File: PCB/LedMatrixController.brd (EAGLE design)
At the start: 100 x 80 mm, 9 parts, among them IC1 AT90S2313S, IC2 74LS595D

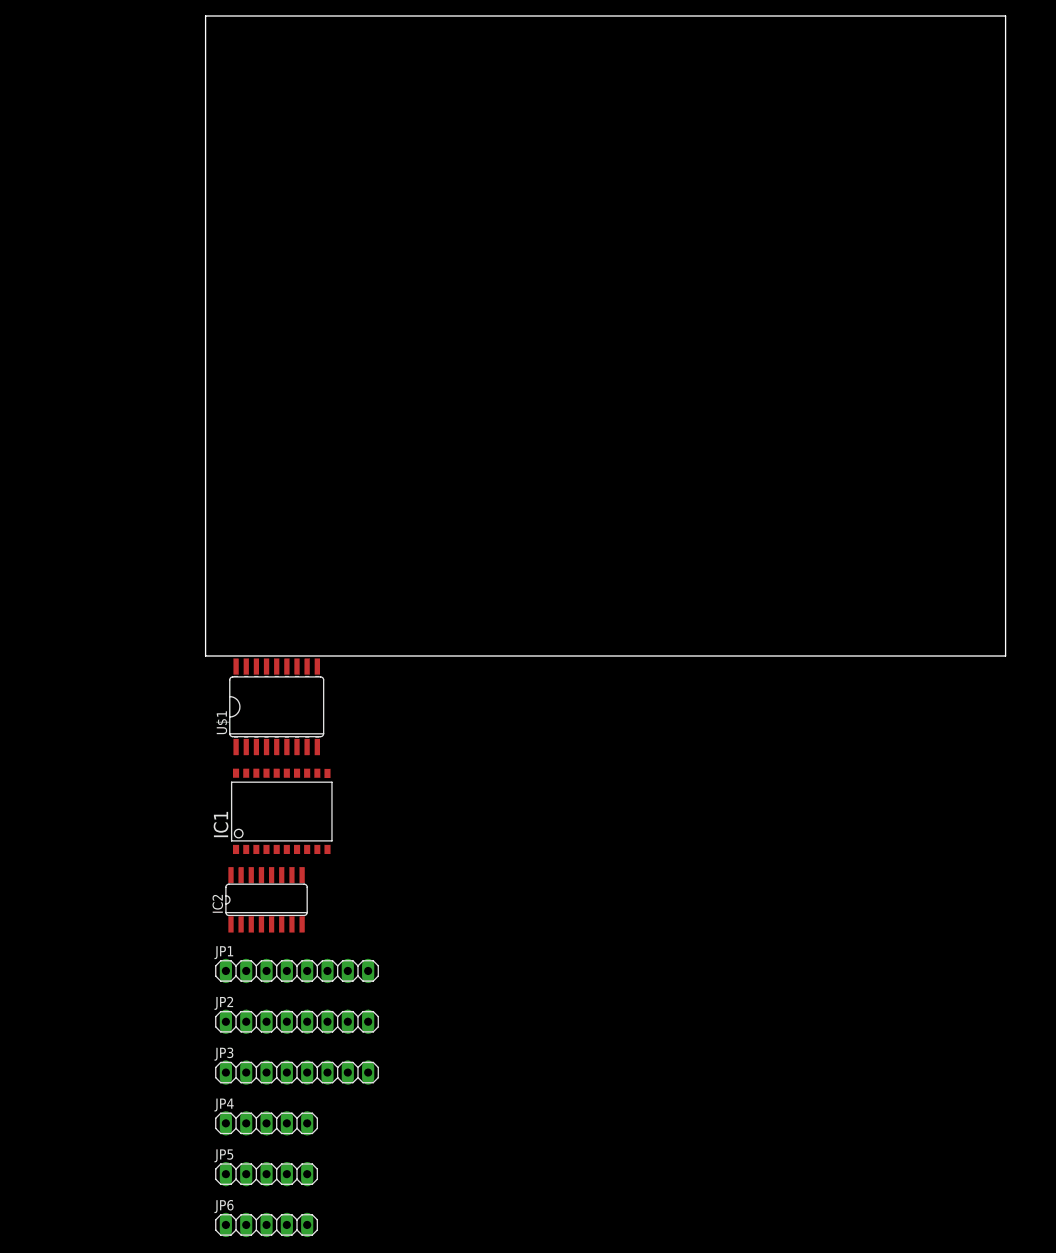
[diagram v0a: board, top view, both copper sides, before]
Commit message: Added connections between main elements. Created dimensions on the pbc layout.
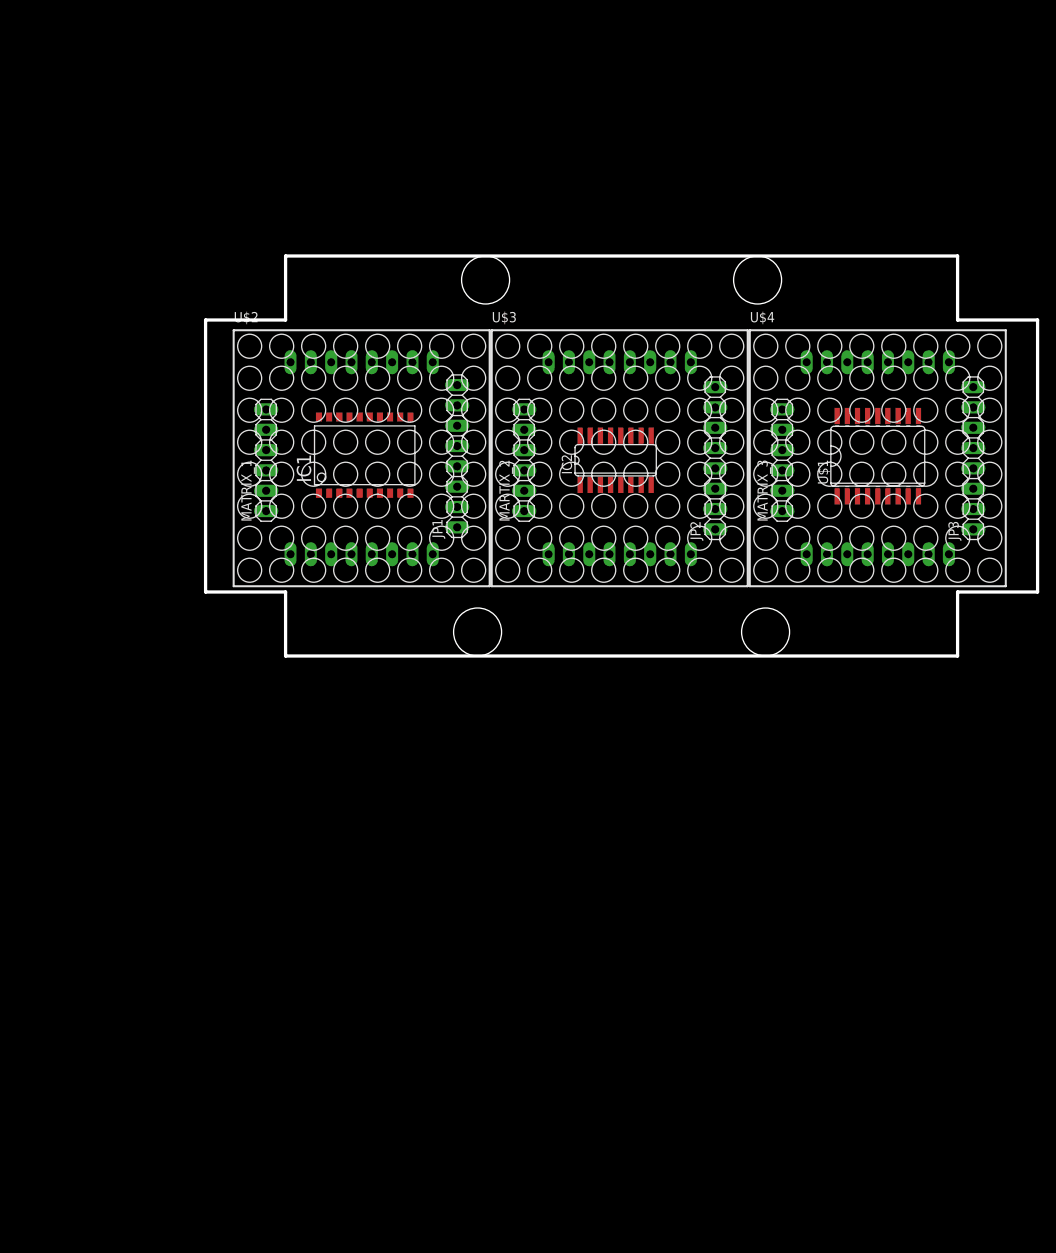
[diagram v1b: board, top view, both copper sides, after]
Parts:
- removed JP4, JP5, JP6: (no value), pinhead:1X05
- added MARTIX_2, MATRIX_1, MATRIX_3: (no value), pinhead:1X06
- added U$2, U$3, U$4: NFM-12881BG-11, led_matrix_8x8:NFM-12881BG-11
- moved JP3 114.2 mm to (96.0, 24.7), turned to 90 degrees
- moved JP2 87.7 mm to (63.7, 24.7), turned to 90 degrees
- moved U$1 81.4 mm to (84.0, 25.0)
- moved IC2 70.2 mm to (51.3, 24.5)
- moved JP1 67.4 mm to (31.4, 25.0), turned to 90 degrees
- moved IC1 45.7 mm to (19.3, 25.5)
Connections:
- new net CLK: IC1.11, MARTIX_2.4, MATRIX_1.4, MATRIX_3.4
- new net N$10: MARTIX_2.3, MATRIX_1.6
- new net N$11: MARTIX_2.6, MATRIX_3.3
- new net N$12: IC1.9, MATRIX_1.3
- new net N$9: IC1.8, MARTIX_2.5, MATRIX_1.5, MATRIX_3.5
- new net R1: IC2.15, U$1.1
- new net R2: IC2.1, U$1.2
- new net R3: IC2.2, U$1.3
- new net R4: IC2.3, U$1.4
- new net R5: IC2.4, U$1.5
- new net R6: IC2.5, U$1.6
- new net R7: IC2.6, U$1.7
- new net R8: IC2.7, U$1.8
- new net ROW1: JP1.1, JP2.1, JP3.1, U$1.10
- new net ROW2: JP1.2, JP2.2, JP3.2, U$1.11
- new net ROW3: JP1.3, JP2.3, JP3.3, U$1.12
- new net ROW4: JP1.4, JP2.4, JP3.4, U$1.13
- new net ROW5: JP1.5, JP2.5, JP3.5, U$1.14
- new net ROW6: JP1.6, JP2.6, JP3.6, U$1.15
- new net ROW7: JP1.7, JP2.7, JP3.7, U$1.16
- new net ROW8: JP1.8, JP2.8, JP3.8, U$1.17
- net GND: now also MARTIX_2.1, MATRIX_1.1, MATRIX_3.1, U$1.9
- net VCC: now also MARTIX_2.2, MATRIX_1.2, MATRIX_3.2
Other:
- board size 100 x 80 mm -> 104 x 50 mm

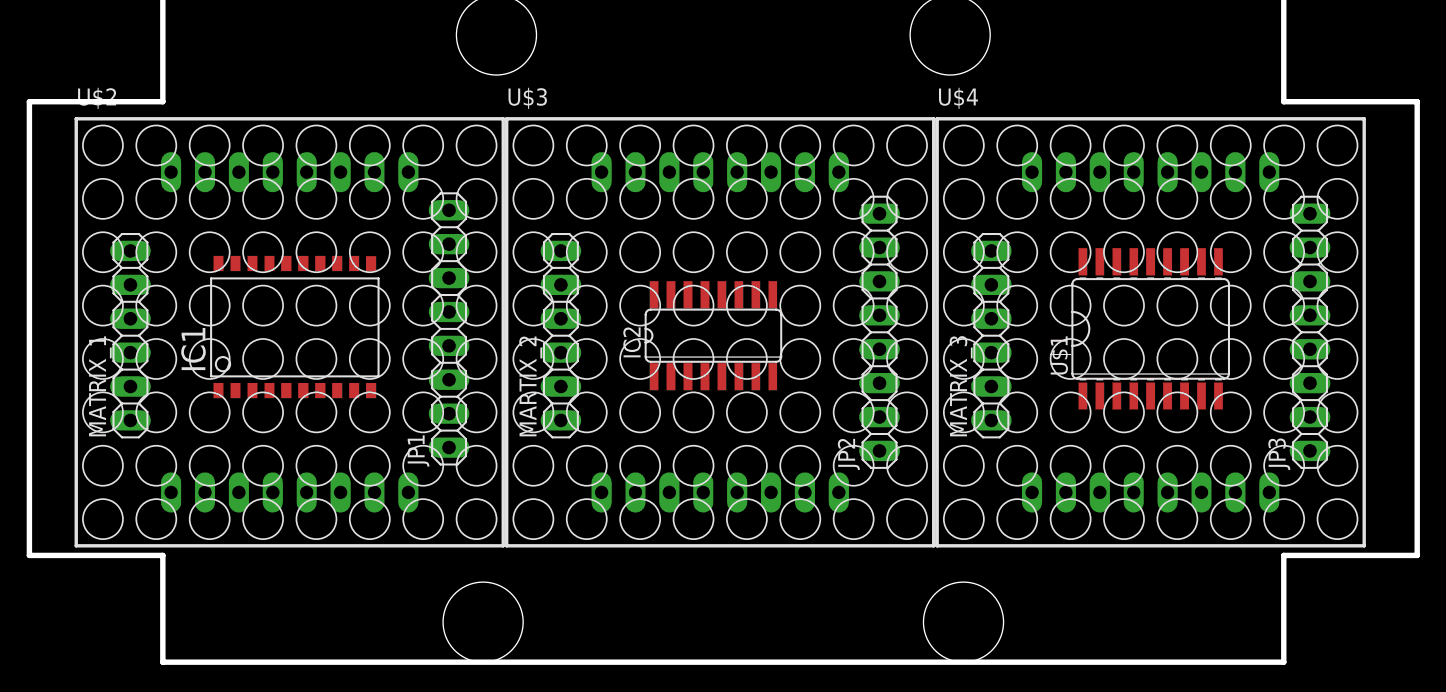
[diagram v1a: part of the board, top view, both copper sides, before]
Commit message: Corrected positions of pinheads on the matrix controller board.
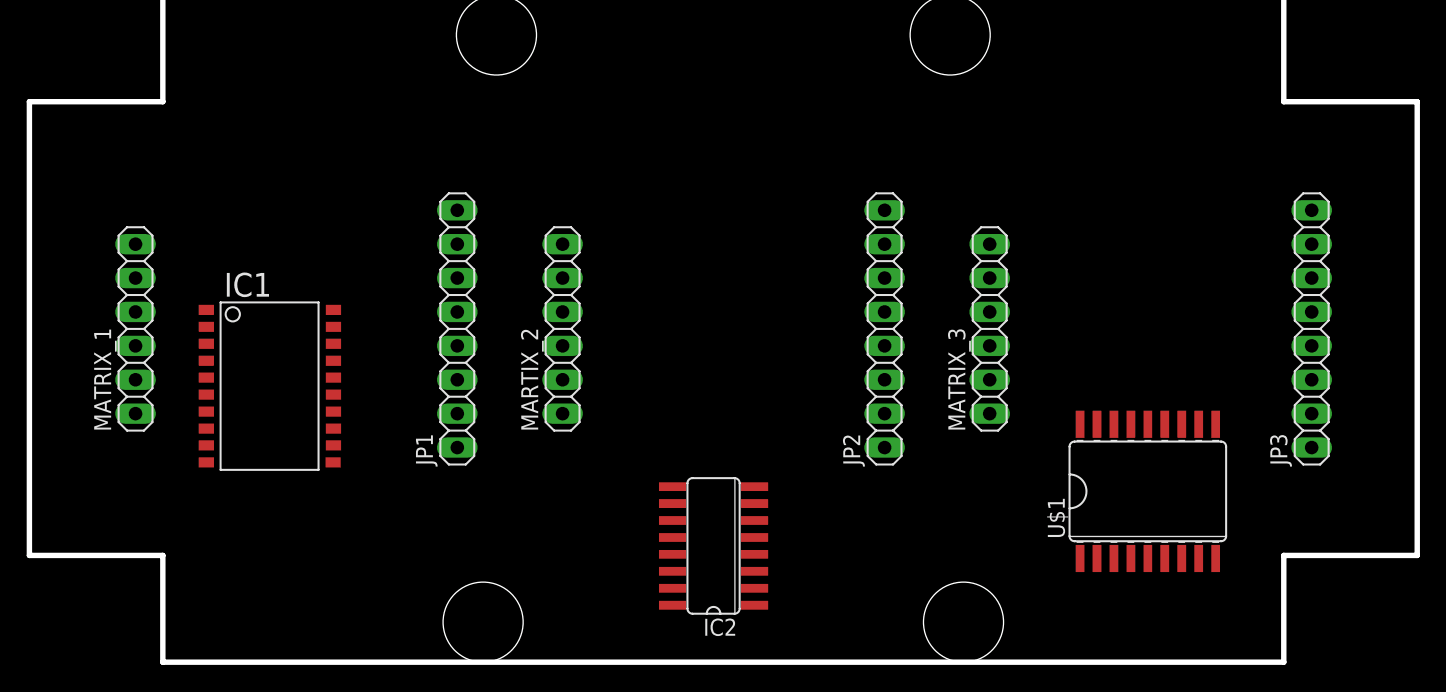
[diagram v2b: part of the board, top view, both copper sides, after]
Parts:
- removed U$2, U$3, U$4: NFM-12881BG-11, led_matrix_8x8:NFM-12881BG-11
- moved IC2 15.8 mm to (51.3, 8.71), turned to 90 degrees
- moved U$1 12.2 mm to (83.8, 12.8)
- moved IC1 4.25 mm to (18.4, 21.3), turned to 270 degrees
- moved MATRIX_1 0.63 mm to (7.95, 25.0)
- moved JP1 0.62 mm to (32.1, 25.0)
- moved MARTIX_2 0.52 mm to (40.0, 25.0)
- moved MATRIX_3 0.52 mm to (72.0, 25.0)
- moved JP2 0.46 mm to (64.1, 25.0)
- moved JP3 0.28 mm to (96.1, 25.0)

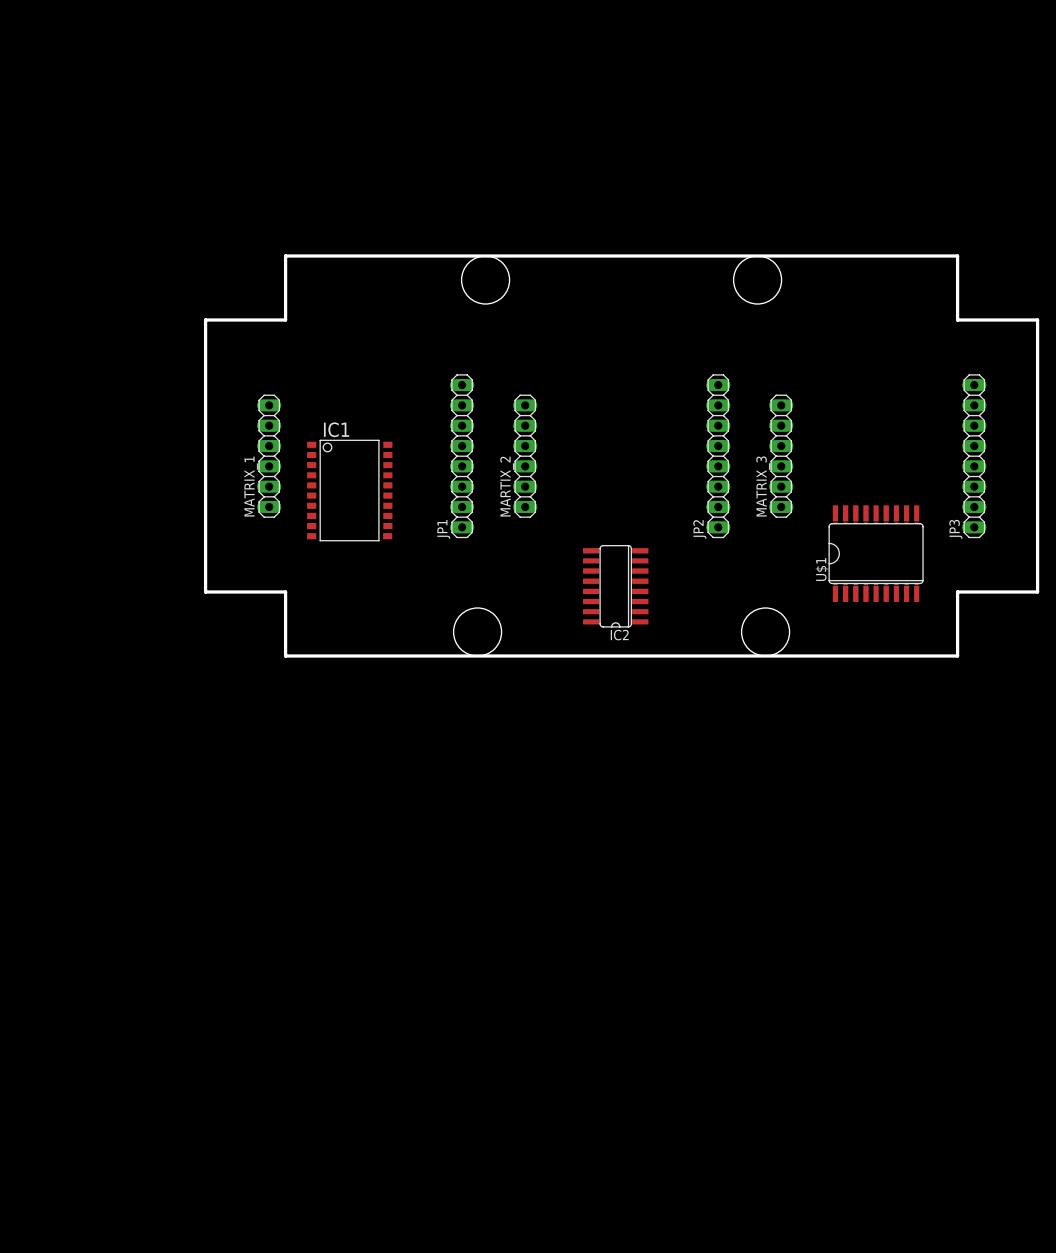
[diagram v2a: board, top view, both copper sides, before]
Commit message: Another part of improvements in pcb layouts. Especially in pinhead area, to match both pcbs.
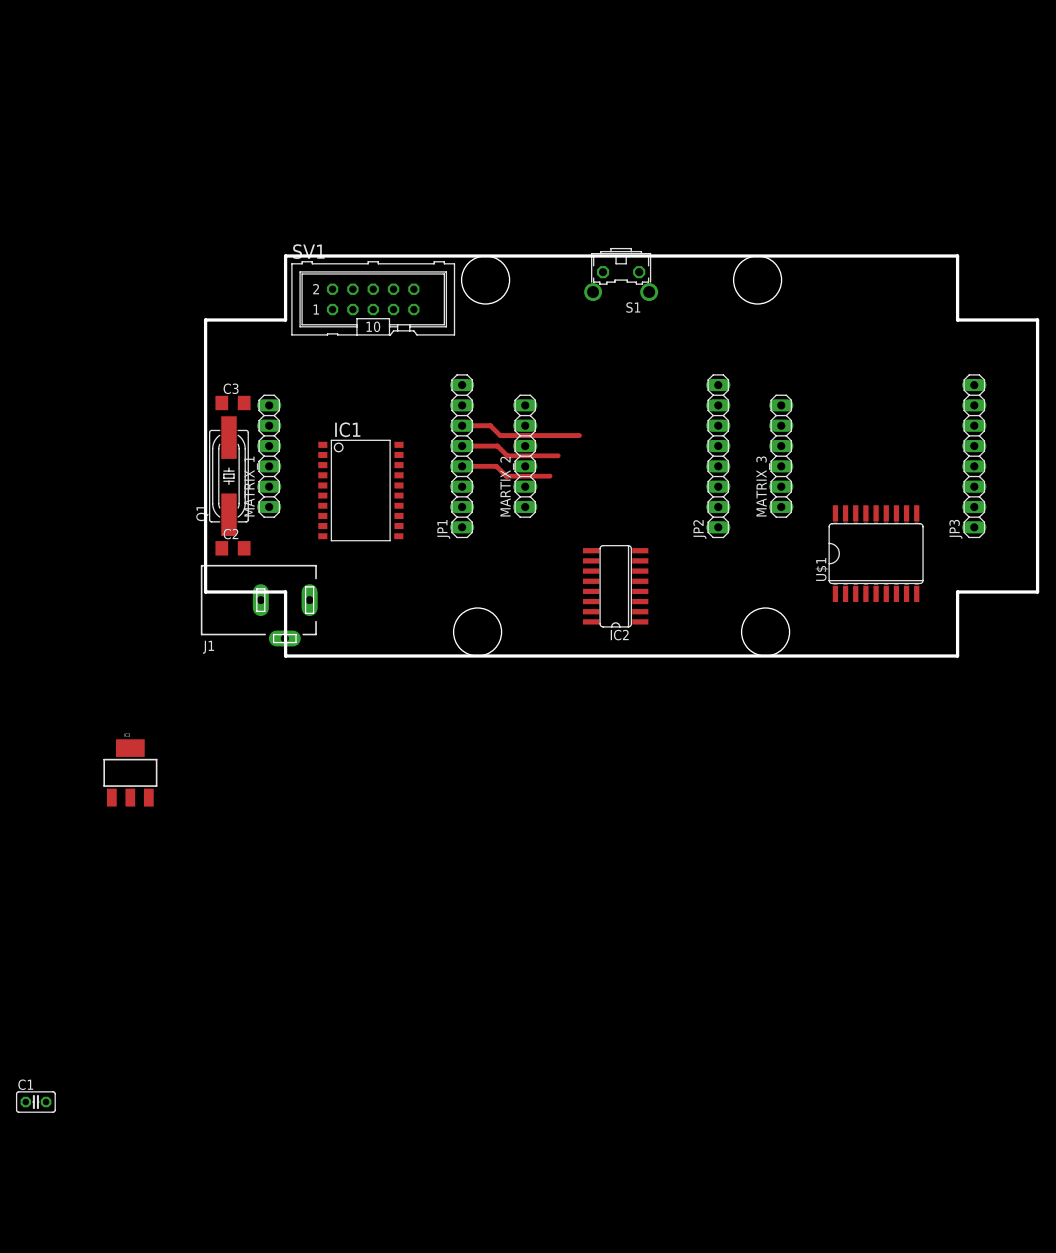
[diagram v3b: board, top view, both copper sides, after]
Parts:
- added C1: (no value), resistor:C025-025X050
- added C2, C3: (no value), resistor:C1206
- added IC3: (no value), SparkFun-PowerIC:SOT223
- added J1: (no value), con-jack:DCJ0303
- added Q1: (no value), crystal:HC49UP
- added S1: (no value), switch-omron:B3F-31XX
- added SV1: (no value), con-ml:ML10
- moved IC1 1.40 mm to (19.8, 21.3)
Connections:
- removed net CLK: IC1.11, MARTIX_2.4, MATRIX_1.4, MATRIX_3.4
- removed net N$10: MARTIX_2.3, MATRIX_1.6
- removed net N$11: MARTIX_2.6, MATRIX_3.3
- removed net N$12: IC1.9, MATRIX_1.3
- removed net N$9: IC1.8, MARTIX_2.5, MATRIX_1.5, MATRIX_3.5
- removed net VCC: IC1.20, IC2.16, MARTIX_2.2, MATRIX_1.2, MATRIX_3.2
- new net +5V: C1.1, IC1.20, IC2.16, IC3.2, IC3.4, MARTIX_2.2, MATRIX_1.2, MATRIX_3.2
- new net COL_CLK: IC1.11, MARTIX_2.5, MATRIX_1.5, MATRIX_3.5
- new net COL_CLR: IC1.8, MARTIX_2.6, MATRIX_1.6, MATRIX_3.6
- new net COL_DATA: IC1.9, MATRIX_1.4
- new net N$1: C2.1, IC1.4, Q1.1
- new net N$2: IC3.3, J1.1
- new net N$3: C3.1, IC1.5, Q1.2
- new net N$4: IC1.7, S1.1
- new net N$5: S1.2
- new net N$8: MARTIX_2.3, MATRIX_3.4
- new net OUT: MARTIX_2.4, MATRIX_1.3
- net GND: now also C1.2, C2.2, C3.2, IC3.1, J1.2, J1.3
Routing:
- net ROW6: track 0.00 -> 15.2 mm
- net ROW5: track 0.00 -> 12.5 mm
- net ROW4: track 0.00 -> 11.5 mm
